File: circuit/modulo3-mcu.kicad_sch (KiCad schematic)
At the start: 65 parts, among them Q1 BS250, Q2 BS170, T1 PA3, T10 PD1, T11 PD0, T12 PC7, T13 PG6, T14 PC4, T15 PC5, T16 PC6, T2 PD2, T3 PA6, T4 PC0, T5 PC1, T6 PG5, T7 PG4, T8 PG3, T9 PA5, U1 74LVC2G32DC, U10 PWR_CONN, U11 FOOTSWITCH, U13 LM1117 3V3, U2 AVR64DA64, U3 SN74LVC1G17, U4 UPDI, U5 TOUCHSCREEN_240x320, U6 FV1_CONN, U7 DBG_UART, U8 AMPCTRL, Y1 32768Hz

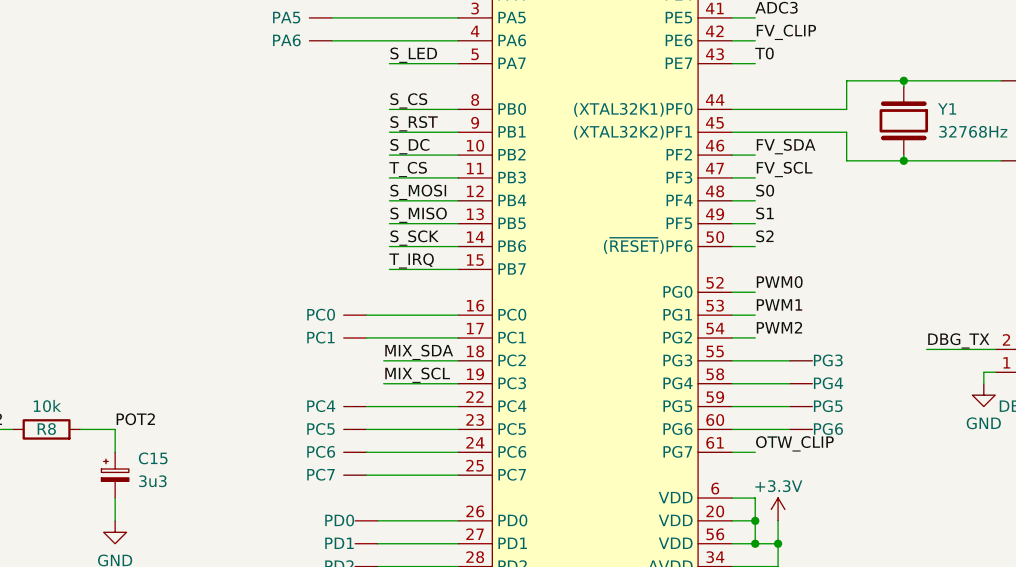
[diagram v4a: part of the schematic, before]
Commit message: lowered the watch resolution to .24 ms; moved the pins of the display; added pull-ups for mix i2c
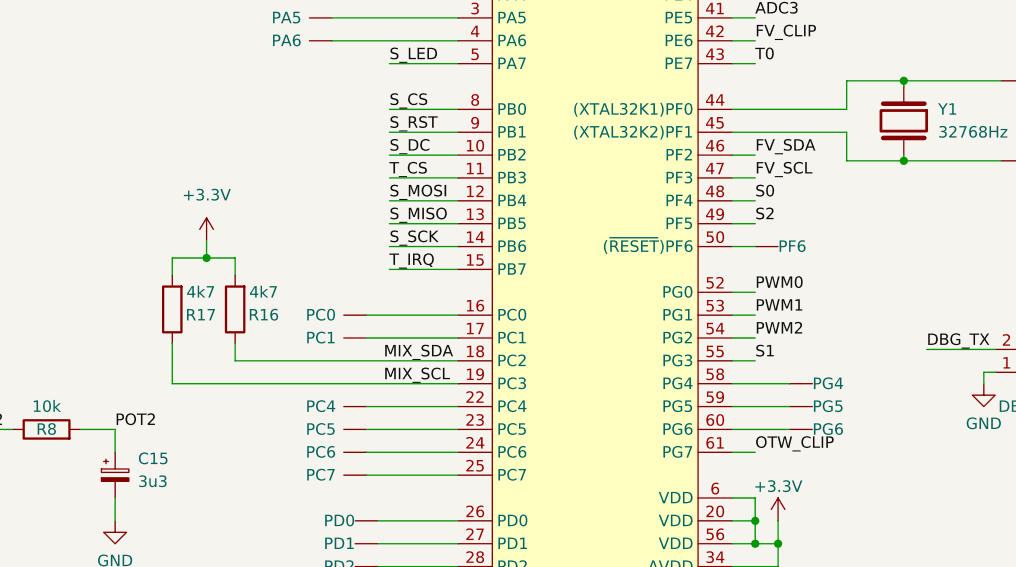
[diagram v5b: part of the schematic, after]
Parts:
- added R16, R17: 4k7, myAmp:R_10MM, symbol myAmp:R
- T8: value PG3 -> PF6
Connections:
- net +3.3V: now also R16.2, R17.2
- net MIX_SCL: now also R17.1
- net MIX_SDA: now also R16.1
- net S1: now also U2.55 (PG3); no longer U2.49 (PF5)
- net S2: now also U2.49 (PF5); no longer U2.50 ((~{RESET})PF6)
- net at T8.1: now also U2.50 ((~{RESET})PF6); no longer U2.55 (PG3)
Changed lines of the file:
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@@
   (junction (at 129.032 181.229) (diameter 0) (color 0 0 0 0)
   )
+  (junction (at 182.88 60.96) (diameter 0) (color 0 0 0 0)
+  )
   (junction (at 246.38 110.49) (diameter 0) (color 0 0 0 0)
   )
@@
   (no_connect (at 34.29 166.37))
   (no_connect (at 34.29 163.83))
+  (wire (pts (xy 179.07 74.93) (xy 179.07 70.485))
+    (stroke (width 0) (type default))
+  )
   (wire (pts (xy 200.66 85.09) (xy 210.82 85.09))
     (stroke (width 0) (type default))
@@
     (stroke (width 0) (type default))
   )
-  (wire (pts (xy 241.3 72.39) (xy 247.65 72.39))
+  (wire (pts (xy 241.3 72.39) (xy 243.84 72.39))
     (stroke (width 0) (type default))
   )
@@
     (stroke (width 0) (type default))
   )
-  (wire (pts (xy 202.565 74.93) (xy 210.82 74.93))
+  (wire (pts (xy 179.07 74.93) (xy 210.82 74.93))
     (stroke (width 0) (type default))
   )
@@
     (stroke (width 0) (type default))
   )
+  (wire (pts (xy 186.055 60.96) (xy 186.055 62.865))
+    (stroke (width 0) (type default))
+  )
   (wire (pts (xy 203.2 100.33) (xy 210.82 100.33))
     (stroke (width 0) (type default))
@@
     (stroke (width 0) (type default))
   )
+  (wire (pts (xy 179.07 62.865) (xy 179.07 60.96))
+    (stroke (width 0) (type default))
+  )
   (wire (pts (xy 49.53 134.62) (xy 53.34 134.62))
     (stroke (width 0) (type default))
@@
     (stroke (width 0) (type default))
   )
+  (wire (pts (xy 182.88 60.96) (xy 186.055 60.96))
+    (stroke (width 0) (type default))
+  )
   (wire (pts (xy 72.39 82.55) (xy 72.39 81.28))
     (stroke (width 0) (type default))
@@
     (stroke (width 0) (type default))
   )
-  (wire (pts (xy 202.565 72.39) (xy 210.82 72.39))
-    (stroke (width 0) (type default))
-  )
   (wire (pts (xy 281.94 50.165) (xy 276.225 50.165))
     (stroke (width 0) (type default))
@@
     (stroke (width 0) (type default))
   )
+  (wire (pts (xy 179.07 60.96) (xy 182.88 60.96))
+    (stroke (width 0) (type default))
+  )
   (wire (pts (xy 241.3 105.41) (xy 246.38 105.41))
     (stroke (width 0) (type default))
@@
     (stroke (width 0) (type default))
   )
+  (wire (pts (xy 182.88 59.055) (xy 182.88 60.96))
+    (stroke (width 0) (type default))
+  )
   (wire (pts (xy 118.237 181.229) (xy 118.237 183.134))
     (stroke (width 0) (type default))
@@
     (stroke (width 0) (type default))
   )
+  (wire (pts (xy 186.055 72.39) (xy 186.055 70.485))
+    (stroke (width 0) (type default))
+  )
   (wire (pts (xy 241.3 31.75) (xy 243.84 31.75))
     (stroke (width 0) (type default))
@@
     (stroke (width 0) (type default))
   )
+  (wire (pts (xy 186.055 72.39) (xy 210.82 72.39))
+    (stroke (width 0) (type default))
+  )
   (wire (pts (xy 144.78 87.63) (xy 144.78 90.17))
     (stroke (width 0) (type default))
@@
     (effects (font (size 1.27 1.27)) (justify left bottom))
   )
-  (label "S2" (at 243.84 59.69 0) (fields_autoplaced)
+  (label "S2" (at 243.84 57.15 0) (fields_autoplaced)
     (effects (font (size 1.27 1.27)) (justify left bottom))
   )
@@
     (effects (font (size 1.27 1.27)) (justify left bottom))
   )
-  (label "S1" (at 243.84 57.15 0) (fields_autoplaced)
+  (label "S1" (at 243.84 72.39 0) (fields_autoplaced)
     (effects (font (size 1.27 1.27)) (justify left bottom))
   )
@@
     )
   )
+  (symbol (lib_id "power:+3.3V") (at 182.88 59.055 0) (unit 1)
+    (in_bom yes) (on_board yes) (dnp no) (fields_autoplaced)
+    (property "Reference" "#PWR020" (at 182.88 62.865 0)
+      (effects (font (size 1.27 1.27)) hide)
+    )
+    (property "Value" "+3.3V" (at 182.88 53.975 0)
+      (effects (font (size 1.27 1.27)))
+    )
+    (property "Footprint" "" (at 182.88 59.055 0)
+      (effects (font (size 1.27 1.27)) hide)
+    )
+    (property "Datasheet" "" (at 182.88 59.055 0)
+      (effects (font (size 1.27 1.27)) hide)
+    )
+    (pin "1")
+    (instances
+      (project "modulo3-mcu"
+        (path "/0f0bc50f-3b2c-45bf-9734-4d8155cef241"
+          (reference "#PWR020") (unit 1)
+        )
+      )
+    )
+  )
   (symbol (lib_id "myAmp:74LVC2G32DC") (at 26.67 33.02 0) (unit 3)
     (in_bom yes) (on_board yes) (dnp no) (fields_autoplaced)
@@
     )
   )
-  (symbol (lib_id "myAmp:TEST") (at 250.19 72.39 0) (unit 1)
+  (symbol (lib_id "myAmp:TEST") (at 246.38 59.69 0) (unit 1)
     (in_bom yes) (on_board yes) (dnp no)
-    (property "Reference" "T8" (at 251.46 71.755 0)
+    (property "Reference" "T8" (at 247.65 59.055 0)
       (effects (font (size 1.27 1.27)) (justify left) hide)
     )
-    (property "Value" "PG3" (at 250.19 72.39 0)
+    (property "Value" "PF6" (at 246.38 59.69 0)
       (effects (font (size 1.27 1.27)) (justify left))
     )
-    (property "Footprint" "myAmp:TestPad" (at 250.19 72.39 0)
+    (property "Footprint" "myAmp:TestPad" (at 246.38 59.69 0)
       (effects (font (size 1.27 1.27)) hide)
     )
-    (property "Datasheet" "" (at 250.19 72.39 0)
+    (property "Datasheet" "" (at 246.38 59.69 0)
       (effects (font (size 1.27 1.27)) hide)
     )
@@
     )
   )
+  (symbol (lib_id "myAmp:R") (at 179.07 66.675 180) (unit 1)
+    (in_bom yes) (on_board yes) (dnp no)
+    (property "Reference" "R17" (at 182.245 67.31 0)
+      (effects (font (size 1.27 1.27)))
+    )
+    (property "Value" "4k7" (at 182.245 64.77 0)
+      (effects (font (size 1.27 1.27)))
+    )
+    (property "Footprint" "myAmp:R_10MM" (at 180.848 66.675 90)
+      (effects (font (size 1.27 1.27)) hide)
+    )
+    (property "Datasheet" "" (at 179.07 66.675 0)
+      (effects (font (size 1.27 1.27)) hide)
+    )
+    (pin "1")
+    (pin "2")
+    (instances
+      (project "modulo3-mcu"
+        (path "/0f0bc50f-3b2c-45bf-9734-4d8155cef241"
+          (reference "R17") (unit 1)
+        )
+      )
+    )
+  )
   (symbol (lib_id "power:GND") (at 85.09 51.435 0) (unit 1)
     (in_bom yes) (on_board yes) (dnp no) (fields_autoplaced)
@@
         )
       )
+    )
+  )
+  (symbol (lib_id "myAmp:R") (at 186.055 66.675 180) (unit 1)
+    (in_bom yes) (on_board yes) (dnp no)
+    (property "Reference" "R16" (at 189.23 67.31 0)
+      (effects (font (size 1.27 1.27)))
+    )
+    (property "Value" "4k7" (at 189.23 64.77 0)
+      (effects (font (size 1.27 1.27)))
+    )
+    (property "Footprint" "myAmp:R_10MM" (at 187.833 66.675 90)
+      (effects (font (size 1.27 1.27)) hide)
+    )
+    (property "Datasheet" "" (at 186.055 66.675 0)
+      (effects (font (size 1.27 1.27)) hide)
+    )
+    (pin "1")
+    (pin "2")
+    (instances
+      (project "modulo3-mcu"
+        (path "/0f0bc50f-3b2c-45bf-9734-4d8155cef241"
+          (reference "R16") (unit 1)
+        )
+      )
